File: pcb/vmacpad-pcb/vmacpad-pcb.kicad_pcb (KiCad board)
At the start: 2 copper layers, 134.7 x 126.1 mm, 77 parts, among them J1 TYPE-C-31-M12_13, J2 Conn_01x04_Pin, J3 Conn_01x04_Pin, K1 1u, K10 1u, K12 2.25u, K13 1u, K14 1u, K16 1u, K17 1u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

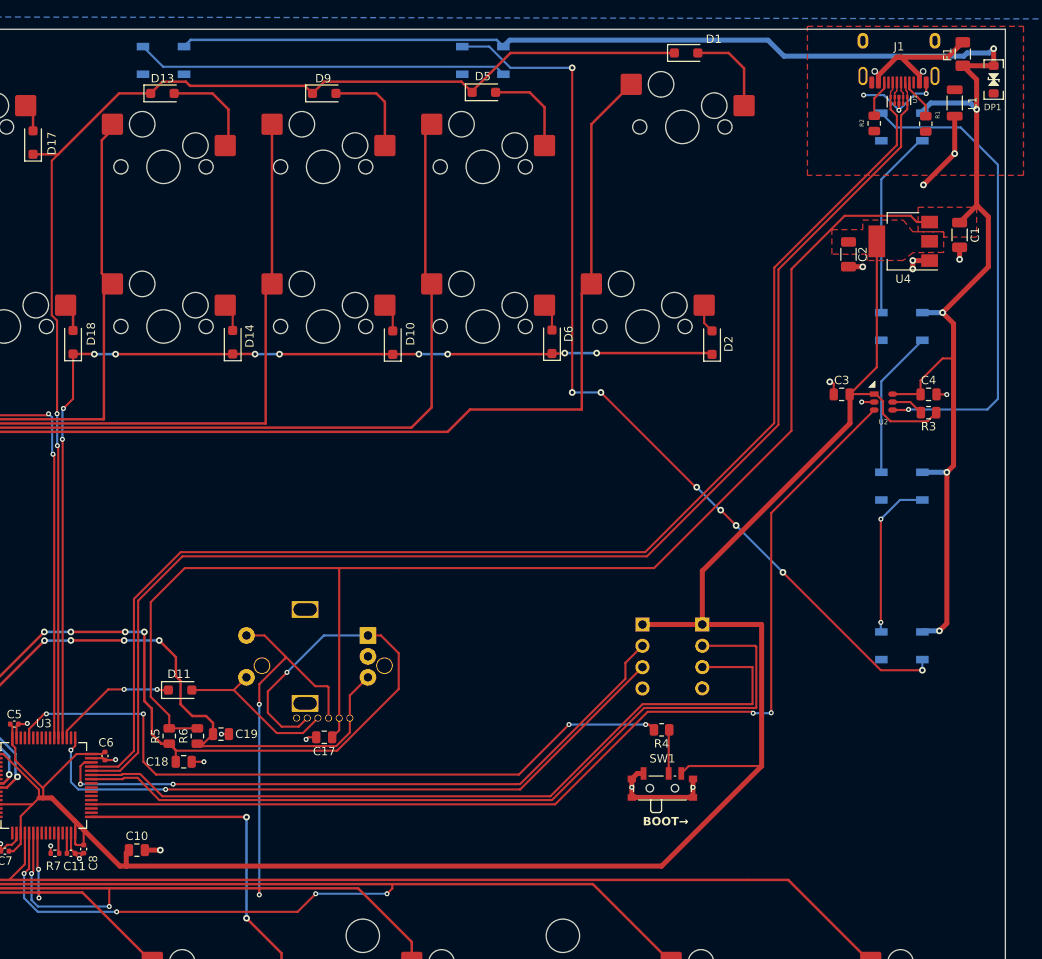
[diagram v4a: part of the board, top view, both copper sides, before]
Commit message: Add tooling holes
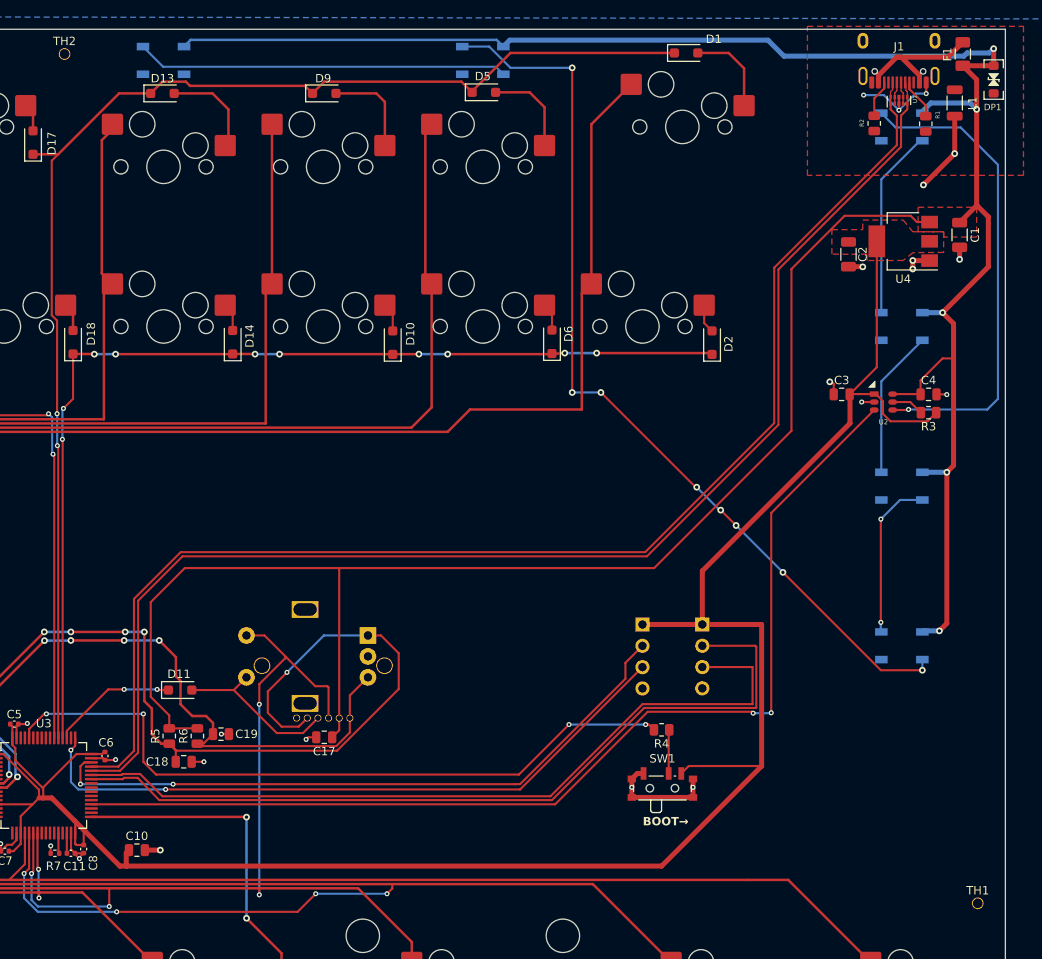
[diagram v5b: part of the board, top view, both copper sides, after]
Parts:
- added TH1: jlcpcb_tooling, max_customs:jlcpcb_tooling, F.Cu at (221.0, 202.2)
- added TH2: jlcpcb_tooling, max_customs:jlcpcb_tooling, F.Cu at (112.0, 100.8)
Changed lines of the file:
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@@
       (plot_on_all_layers_selection 0x0000000_00000000)
       (disableapertmacros false)
-      (usegerberextensions false)
-      (usegerberattributes true)
-      (usegerberadvancedattributes true)
-      (creategerberjobfile true)
+      (usegerberextensions true)
+      (usegerberattributes false)
+      (usegerberadvancedattributes false)
+      (creategerberjobfile false)
       (dashed_line_dash_ratio 12.000000)
       (dashed_line_gap_ratio 3.000000)
@@
       (psa4output false)
       (plotreference true)
-      (plotvalue true)
+      (plotvalue false)
       (plotinvisibletext false)
       (sketchpadsonfab false)
-      (subtractmaskfromsilk false)
+      (subtractmaskfromsilk true)
       (outputformat 1)
       (mirror false)
-      (drillshape 1)
+      (drillshape 0)
       (scaleselection 1)
-      (outputdirectory "")
+      (outputdirectory "../fabrication/")
     )
   )
@@
     (fp_line (start 1 0.625) (end -1 0.625)
       (stroke (width 0.1) (type solid)) (layer "F.Fab"))
-    (pad "1" smd roundrect (at -0.9125 0 90) (size 1.025 1.4) (layers "F.Cu" "F.Paste" "F.Mask") (roundrect_rratio 0.243902)
+    (pad "1" smd roundrect (at -0.9125 0 90) (size 1.025 1.4) (layers "F.Cu" "F.Paste" "F.Mask") (roundrect_rratio 0.243902439)
       (net 30 "BOURNS_PADA") (pintype "passive"))
-    (pad "2" smd roundrect (at 0.9125 0 90) (size 1.025 1.4) (layers "F.Cu" "F.Paste" "F.Mask") (roundrect_rratio 0.243902)
+    (pad "2" smd roundrect (at 0.9125 0 90) (size 1.025 1.4) (layers "F.Cu" "F.Paste" "F.Mask") (roundrect_rratio 0.243902439)
       (net 2 "VCC") (pintype "passive"))
     (model "${KICAD6_3DMODEL_DIR}/Resistor_SMD.3dshapes/R_0805_2012Metric.wrl"
@@
     (fp_line (start 1 0.625) (end -1 0.625)
       (stroke (width 0.1) (type solid)) (layer "F.Fab"))
-    (pad "1" smd roundrect (at -0.9125 0 180) (size 1.025 1.4) (layers "F.Cu" "F.Paste" "F.Mask") (roundrect_rratio 0.243902)
+    (pad "1" smd roundrect (at -0.9125 0 180) (size 1.025 1.4) (layers "F.Cu" "F.Paste" "F.Mask") (roundrect_rratio 0.243902439)
       (net 32 "/SW_BOOT") (pintype "passive"))
-    (pad "2" smd roundrect (at 0.9125 0 180) (size 1.025 1.4) (layers "F.Cu" "F.Paste" "F.Mask") (roundrect_rratio 0.243902)
+    (pad "2" smd roundrect (at 0.9125 0 180) (size 1.025 1.4) (layers "F.Cu" "F.Paste" "F.Mask") (roundrect_rratio 0.243902439)
       (net 16 "/BOOT0") (pintype "passive"))
     (model "${KICAD6_3DMODEL_DIR}/Resistor_SMD.3dshapes/R_0805_2012Metric.wrl"
@@
     (fp_line (start 1 0.625) (end -1 0.625)
       (stroke (width 0.1) (type solid)) (layer "F.Fab"))
-    (pad "1" smd roundrect (at -0.9125 0 270) (size 1.025 1.4) (layers "F.Cu" "F.Paste" "F.Mask") (roundrect_rratio 0.243902)
+    (pad "1" smd roundrect (at -0.9125 0 270) (size 1.025 1.4) (layers "F.Cu" "F.Paste" "F.Mask") (roundrect_rratio 0.243902439)
       (net 7 "Net-(J1-CC2)") (pintype "passive"))
-    (pad "2" smd roundrect (at 0.9125 0 270) (size 1.025 1.4) (layers "F.Cu" "F.Paste" "F.Mask") (roundrect_rratio 0.243902)
+    (pad "2" smd roundrect (at 0.9125 0 270) (size 1.025 1.4) (layers "F.Cu" "F.Paste" "F.Mask") (roundrect_rratio 0.243902439)
       (net 4 "GNDPWR") (pintype "passive"))
     (model "${KICAD6_3DMODEL_DIR}/Resistor_SMD.3dshapes/R_0805_2012Metric.wrl"
@@
     (fp_line (start 1 0.625) (end -1 0.625)
       (stroke (width 0.1) (type solid)) (layer "F.Fab"))
-    (pad "1" smd roundrect (at -0.9125 0 270) (size 1.025 1.4) (layers "F.Cu" "F.Paste" "F.Mask") (roundrect_rratio 0.243902)
+    (pad "1" smd roundrect (at -0.9125 0 270) (size 1.025 1.4) (layers "F.Cu" "F.Paste" "F.Mask") (roundrect_rratio 0.243902439)
       (net 5 "Net-(J1-CC1)") (pintype "passive"))
-    (pad "2" smd roundrect (at 0.9125 0 270) (size 1.025 1.4) (layers "F.Cu" "F.Paste" "F.Mask") (roundrect_rratio 0.243902)
+    (pad "2" smd roundrect (at 0.9125 0 270) (size 1.025 1.4) (layers "F.Cu" "F.Paste" "F.Mask") (roundrect_rratio 0.243902439)
       (net 4 "GNDPWR") (pintype "passive"))
     (model "${KICAD6_3DMODEL_DIR}/Resistor_SMD.3dshapes/R_0805_2012Metric.wrl"
@@
     (fp_line (start 1.6 0.8) (end -1.6 0.8)
       (stroke (width 0.1) (type solid)) (layer "F.Fab"))
-    (pad "1" smd roundrect (at -1.475 0 270) (size 1.15 1.8) (layers "F.Cu" "F.Paste" "F.Mask") (roundrect_rratio 0.217391)
+    (pad "1" smd roundrect (at -1.475 0 270) (size 1.15 1.8) (layers "F.Cu" "F.Paste" "F.Mask") (roundrect_rratio 0.2173913043)
       (net 2 "VCC") (pintype "passive"))
-    (pad "2" smd roundrect (at 1.475 0 270) (size 1.15 1.8) (layers "F.Cu" "F.Paste" "F.Mask") (roundrect_rratio 0.217391)
+    (pad "2" smd roundrect (at 1.475 0 270) (size 1.15 1.8) (layers "F.Cu" "F.Paste" "F.Mask") (roundrect_rratio 0.2173913043)
       (net 3 "GND") (pintype "passive"))
     (model "${KICAD6_3DMODEL_DIR}/Capacitor_SMD.3dshapes/C_1206_3216Metric.wrl"
@@
     )
   )
+  (footprint "max_customs:jlcpcb_tooling" (layer "F.Cu")
+    (at 112.014 100.838)
+    (attr through_hole)
+    (fp_text reference "TH2" (at 0 -1.524 unlocked) (layer "F.SilkS")
+        (effects (font (size 1 1) (thickness 0.15)))
+    )
+    (fp_text value "jlcpcb_tooling" (at 0 -2 unlocked) (layer "F.Fab")
+        (effects (font (size 1 1) (thickness 0.15)))
+    )
+    (pad "1" thru_hole circle (at 0 0) (size 1.4 1.4) (drill 1.152) (layers "*.Cu" "*.Mask"))
+  )
   (footprint "acheron_MXH:MX100H" (layer "F.Cu")
     (at 128.5875 214.3125)
@@
     (fp_line (start 1.6 0.8) (end -1.6 0.8)
       (stroke (width 0.1) (type solid)) (layer "F.Fab"))
-    (pad "1" smd roundrect (at -1.575 0 90) (size 1.05 1.9) (layers "F.Cu" "F.Paste" "F.Mask") (roundrect_rratio 0.238095)
+    (pad "1" smd roundrect (at -1.575 0 90) (size 1.05 1.9) (layers "F.Cu" "F.Paste" "F.Mask") (roundrect_rratio 0.2380952381)
       (net 3 "GND") (pinfunction "1") (pintype "passive"))
-    (pad "2" smd roundrect (at 1.575 0 90) (size 1.05 1.9) (layers "F.Cu" "F.Paste" "F.Mask") (roundrect_rratio 0.238095)
+    (pad "2" smd roundrect (at 1.575 0 90) (size 1.05 1.9) (layers "F.Cu" "F.Paste" "F.Mask") (roundrect_rratio 0.2380952381)
       (net 4 "GNDPWR") (pinfunction "2") (pintype "passive"))
     (model "${KICAD6_3DMODEL_DIR}/Inductor_SMD.3dshapes/L_1206_3216Metric.wrl"
@@
     (fp_line (start 1 0.625) (end -1 0.625)
       (stroke (width 0.1) (type solid)) (layer "F.Fab"))
-    (pad "1" smd roundrect (at -0.9125 0 90) (size 1.025 1.4) (layers "F.Cu" "F.Paste" "F.Mask") (roundrect_rratio 0.243902)
+    (pad "1" smd roundrect (at -0.9125 0 90) (size 1.025 1.4) (layers "F.Cu" "F.Paste" "F.Mask") (roundrect_rratio 0.243902439)
       (net 61 "BOURNS_PADB") (pintype "passive"))
-    (pad "2" smd roundrect (at 0.9125 0 90) (size 1.025 1.4) (layers "F.Cu" "F.Paste" "F.Mask") (roundrect_rratio 0.243902)
+    (pad "2" smd roundrect (at 0.9125 0 90) (size 1.025 1.4) (layers "F.Cu" "F.Paste" "F.Mask") (roundrect_rratio 0.243902439)
       (net 2 "VCC") (pintype "passive"))
     (model "${KICAD6_3DMODEL_DIR}/Resistor_SMD.3dshapes/R_0805_2012Metric.wrl"
@@
     (fp_line (start 1 0.625) (end -1 0.625)
       (stroke (width 0.1) (type solid)) (layer "F.Fab"))
-    (pad "1" smd roundrect (at -0.9125 0 180) (size 1.025 1.4) (layers "F.Cu" "F.Paste" "F.Mask") (roundrect_rratio 0.243902)
+    (pad "1" smd roundrect (at -0.9125 0 180) (size 1.025 1.4) (layers "F.Cu" "F.Paste" "F.Mask") (roundrect_rratio 0.243902439)
       (net 9 "+3.3V") (pintype "passive"))
-    (pad "2" smd roundrect (at 0.9125 0 180) (size 1.025 1.4) (layers "F.Cu" "F.Paste" "F.Mask") (roundrect_rratio 0.243902)
+    (pad "2" smd roundrect (at 0.9125 0 180) (size 1.025 1.4) (layers "F.Cu" "F.Paste" "F.Mask") (roundrect_rratio 0.243902439)
       (net 54 "Net-(U2-OE)") (pintype "passive"))
     (model "${KICAD6_3DMODEL_DIR}/Resistor_SMD.3dshapes/R_0805_2012Metric.wrl"
@@
     )
   )
+  (footprint "max_customs:jlcpcb_tooling" (layer "F.Cu")
+    (at 220.98 202.184)
+    (attr through_hole)
+    (fp_text reference "TH1" (at 0 -1.524 unlocked) (layer "F.SilkS")
+        (effects (font (size 1 1) (thickness 0.15)))
+    )
+    (fp_text value "jlcpcb_tooling" (at 0 -2 unlocked) (layer "F.Fab")
+        (effects (font (size 1 1) (thickness 0.15)))
+    )
+    (pad "1" thru_hole circle (at 0 0) (size 1.4 1.4) (drill 1.152) (layers "*.Cu" "*.Mask"))
+  )
   (footprint "Diode_SMD:D_SOD-123F" (layer "F.Cu")
     (at 159.9692 222.4024)
@@
     (fp_line (start 1.6 0.8) (end -1.6 0.8)
       (stroke (width 0.1) (type solid)) (layer "F.Fab"))
-    (pad "1" smd roundrect (at -1.475 0 270) (size 1.15 1.8) (layers "F.Cu" "F.Paste" "F.Mask") (roundrect_rratio 0.217391)
+    (pad "1" smd roundrect (at -1.475 0 270) (size 1.15 1.8) (layers "F.Cu" "F.Paste" "F.Mask") (roundrect_rratio 0.2173913043)
       (net 9 "+3.3V") (pintype "passive"))
-    (pad "2" smd roundrect (at 1.475 0 270) (size 1.15 1.8) (layers "F.Cu" "F.Paste" "F.Mask") (roundrect_rratio 0.217391)
+    (pad "2" smd roundrect (at 1.475 0 270) (size 1.15 1.8) (layers "F.Cu" "F.Paste" "F.Mask") (roundrect_rratio 0.2173913043)
       (net 3 "GND") (pintype "passive"))
     (model "${KICAD6_3DMODEL_DIR}/Capacitor_SMD.3dshapes/C_1206_3216Metric.wrl"

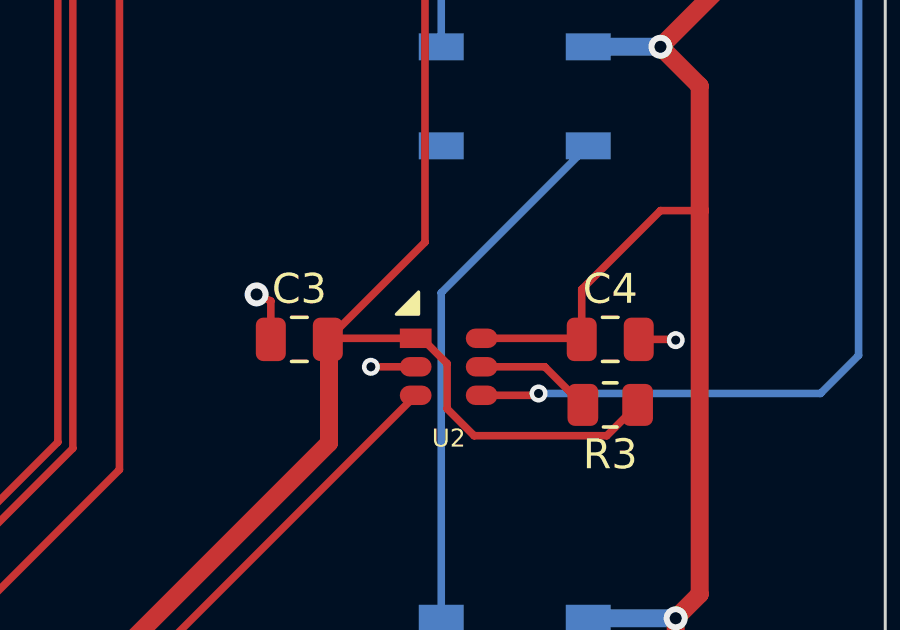
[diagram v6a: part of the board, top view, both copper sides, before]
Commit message: Fixes to part numbers and production
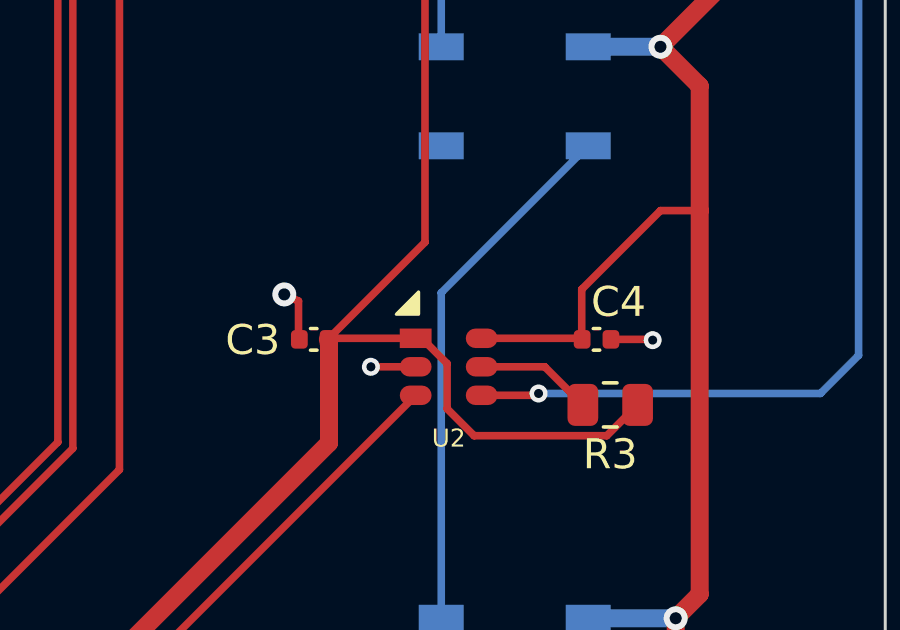
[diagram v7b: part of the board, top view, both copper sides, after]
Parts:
- C3, C4: footprint Capacitor_SMD:C_0805_2012Metric -> Capacitor_SMD:C_0402_1005Metric
- moved C3 0.48 mm to (205.2, 141.5)
- moved C4 0.46 mm to (214.7, 141.5)
